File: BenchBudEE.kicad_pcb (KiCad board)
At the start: 4 copper layers, 165.1 x 63.5 mm, 111 parts, among them K1 RELAY, P1 24 Pin MiniFit JR, P2 CONN_2, P3 CONN_3X2, P4 12 Pin Terminal Block, P5 CONN_3, Q1 2N3904, Q2 MOSFET_N, Q3 NMOS, Q4 NMOS, SW1 SWITCH, U1 OPTO_TRANSISTOR, U10 LM317K, U2 MCP3901, U3 LMT84, U4 OPA4170, U5 AP5726, U6 MCP4801, U7 LM337T, U8 LM317K, U9 LM337T

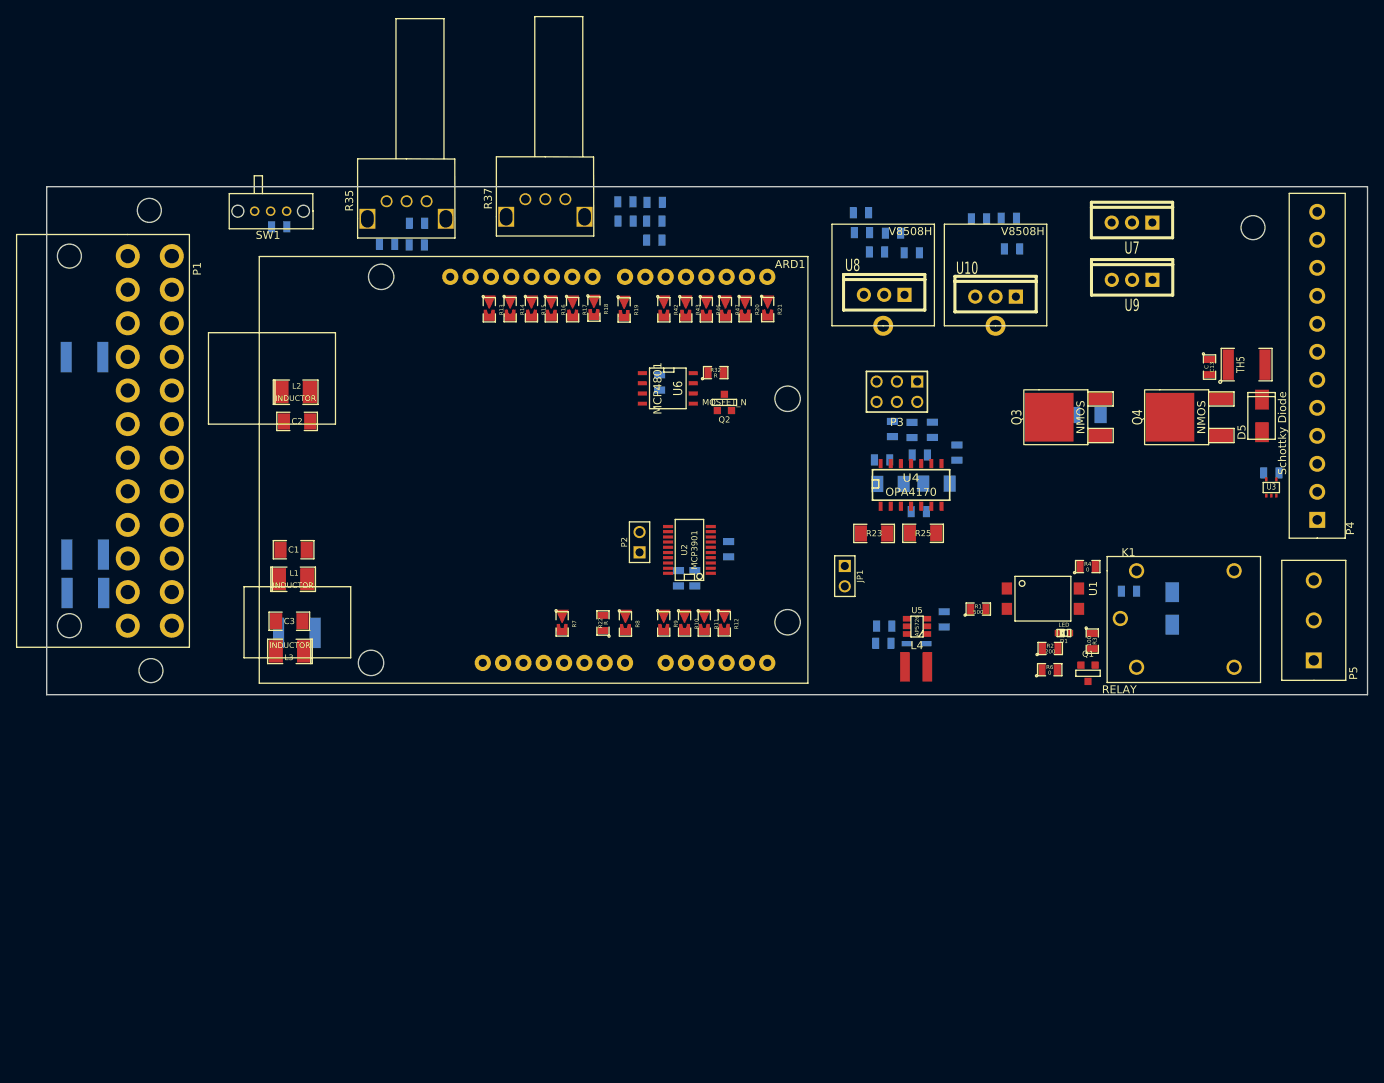
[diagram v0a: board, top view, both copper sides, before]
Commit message: Layout v4.0
Adding ground planes according to location of modules
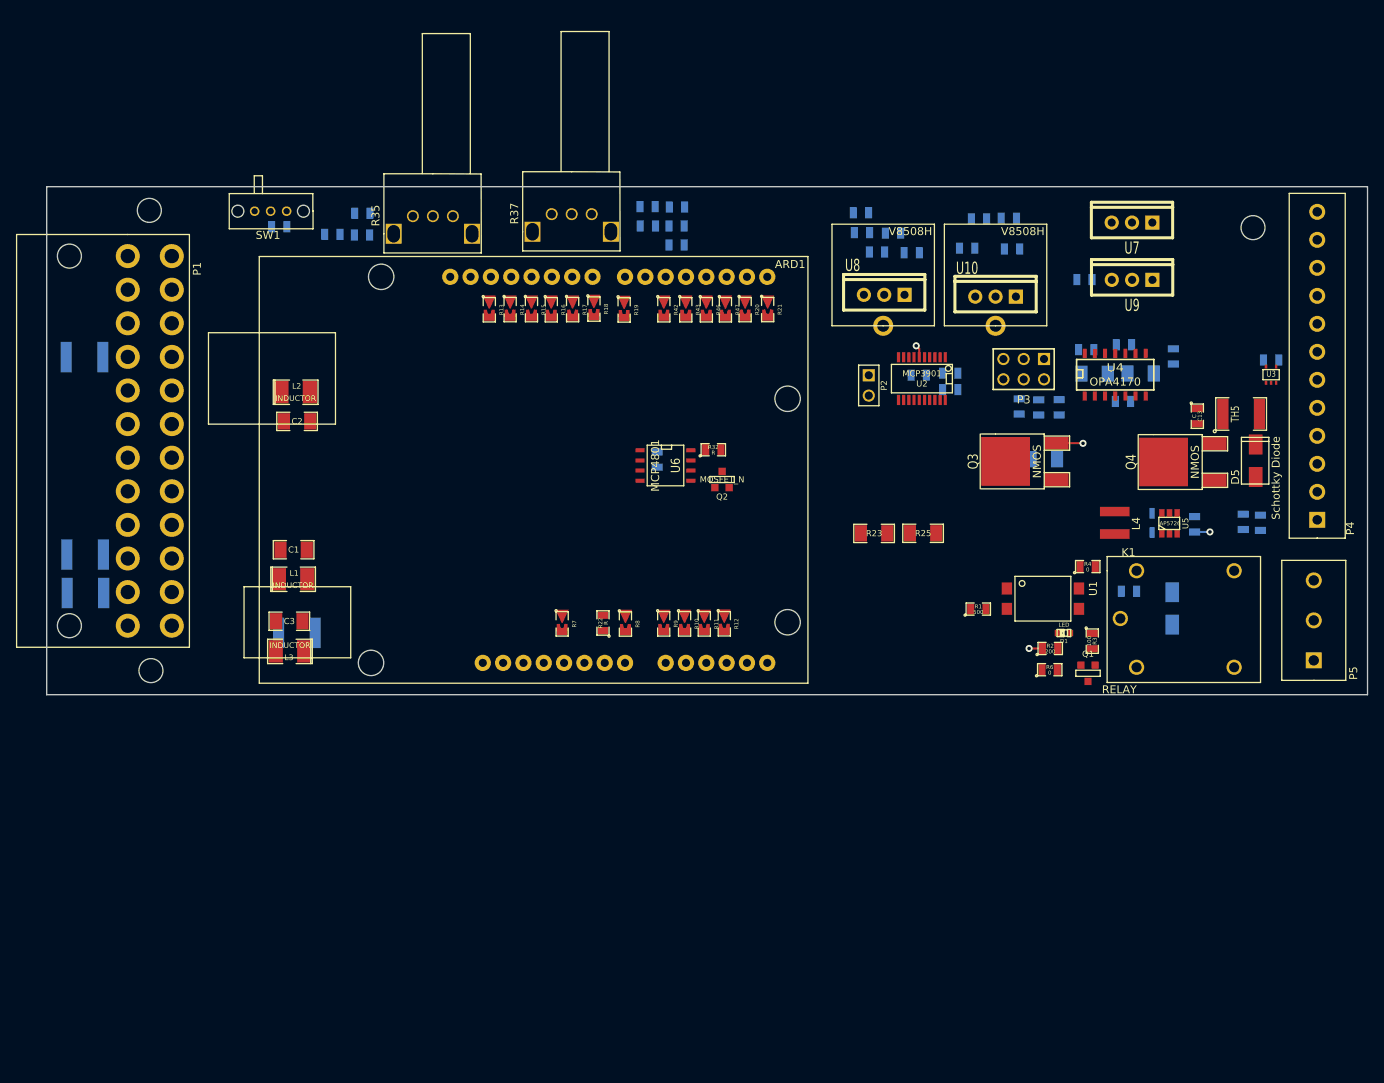
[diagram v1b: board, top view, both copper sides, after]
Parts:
- removed JP1: JUMPER, PIN_ARRAY_2X1
- added C20: C, SM0805, B.Cu at (182.3, 128.8)
- added C21: C, SM0805, B.Cu at (197.0, 132.7)
- moved C5 48.8 mm to (219.0, 163.1), turned to 90 degrees
- moved C4 47.5 mm to (216.9, 163.0), turned to 270 degrees
- moved C7 41.4 mm to (180.2, 146.5), turned to 0 degrees
- moved C6 40.9 mm to (180.2, 144.4), turned to 0 degrees
- moved U2 36.1 mm to (176.7, 145.1), turned to 180 degrees
- moved P2 34.7 mm to (170.0, 146.0), turned to 270 degrees
- moved U5 34.1 mm to (207.6, 163.2), turned to 0 degrees
- moved R31 33.5 mm to (210.8, 163.3)
- moved L4 32.6 mm to (200.8, 161.7), turned to 270 degrees
- moved C8 32.2 mm to (176.3, 144.7), turned to 180 degrees
- moved D4 31.5 mm to (205.5, 164.4), turned to 90 degrees
- moved R27 29.6 mm to (208.1, 142.3)
- moved R26 29.0 mm to (198.3, 144.5)
- moved U4 29.0 mm to (200.8, 144.5)
- moved C10 29.0 mm to (201.8, 148.0)
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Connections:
- C10 pad 2: AGND -> GND_TC
- C11 pad 2: AGND -> GND_TC
- C12 pad 2: AGND -> GND_FAN
- C13 pad 2: GND -> GND_FAN
- C14 pad 2: AGND -> GND_PWR
- C15 pad 2: AGND -> GND_PWR
- C16 pad 1: AGND -> GND_TC
- C17 pad 2: AGND -> GND_TC
- C18 pad 2: AGND -> GND_PWR
- C19 pad 2: AGND -> GND_PWR
- C4 pad 1: GND -> GND_LED
- C5 pad 2: GND -> GND_LED
- C6 pad 2: AGND -> GND_TC
- C7 pad 2: AGND -> GND_TC
- C8 pad 2: AGND -> GND_TC
- C9 pad 2: AGND -> GND_TC
- P4 pad 1: +3.3V -> /LED_Driver/LED+
- P4 pad 10: /Fan/TACH -> +5V
- P4 pad 11: /Terminal_Block/TC_IN_+ -> /Power_Adjustment_Monitor/V-_ADJ
- P4 pad 12: /Terminal_Block/TC_IN_- -> /Power_Adjustment_Monitor/V+_ADJ
- P4 pad 2: +5V -> /LED_Driver/LED-
- P4 pad 3: GND -> /Fan/TACH
- P4 pad 4: /Power_Adjustment_Monitor/V+_ADJ -> /Fan/PWR-
- P4 pad 5: /Power_Adjustment_Monitor/V-_ADJ -> /Fan/PWR+
- P4 pad 6: /LED_Driver/LED+ -> /Terminal_Block/TC_IN_-
- P4 pad 7: /LED_Driver/LED- -> /Terminal_Block/TC_IN_+
- P4 pad 8: /Fan/PWR+ -> GND
- P4 pad 9: /Fan/PWR- -> +3.3V
- Q2 pad S: AGND -> GND_FAN
- Q3 pad 3: GND -> GND_FAN
- R2 pad 1: GND -> GND_RELAY
- R24 pad 1: AGND -> GND_TC
- R31 pad 2: GND -> GND_LED
- R33 pad 2: GND -> GND_FAN
- R35 pad 2: AGND -> GND_PWR
- R37 pad 2: AGND -> GND_PWR
- R39 pad 2: AGND -> GND_PWR
- R41 pad 1: AGND -> GND_PWR
- R48 pad 2: AGND -> GND_TC
- R51 pad 2: AGND -> GND_TC
- R6 pad 1: GND -> GND_RELAY
- U2 pad 11: AGND -> GND_TC
- U2 pad 5: AGND -> GND_TC
- U2 pad 6: AGND -> GND_TC
- U2 pad 8: AGND -> GND_TC
- U3 pad 1: AGND -> GND_TC
- U3 pad 2: AGND -> GND_TC
- U3 pad 5: AGND -> GND_TC
- U5 pad 2: GND -> GND_LED
- U6 pad 7: AGND -> GND_FAN
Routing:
- net GND_FAN: track 0.00 -> 4.88 mm, vias 0 -> 1
- net GND_RELAY: track 0.00 -> 3.11 mm, vias 0 -> 1
- net GND_LED: track 0.00 -> 2.90 mm, vias 0 -> 1
- net GND_TC: track 0.00 -> 2.47 mm, vias 0 -> 1
- added copper zone on GND, net GND_FAN
- added copper zone on GND, net GND_LED
- added copper zone on GND, net GND_PWR
- added copper zone on GND, net GND_RELAY
- added copper zone on GND, net GND_TC

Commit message: Layout v5.0
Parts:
- added TP1: CONN_1, 1pin, F.Cu at (120.9, 160.5)
- C13, TH5: moved to B.Cu
- C4: moved to F.Cu
- moved C3 47.5 mm to (94.7, 128.0), turned to 0 degrees
- moved TH3 41.0 mm to (89.8, 179.3), turned to 0 degrees
- moved U9 33.2 mm to (169.8, 130.9), turned to 270 degrees
- moved U8 29.5 mm to (201.4, 136.4)
- moved C12 26.6 mm to (170.1, 153.8)
- moved R32 26.6 mm to (177.2, 152.6)
- moved U6 26.6 mm to (171.2, 154.6)
- moved Q2 26.6 mm to (178.2, 156.3)
- moved TH2 25.8 mm to (97.7, 163.7), turned to 0 degrees
- moved C2 18.3 mm to (94.7, 132.6)
- moved TH5 15.5 mm to (202.5, 155.9), turned to 90 degrees
- moved U7 15.2 mm to (213.7, 136.4)
- moved C13 14.3 mm to (198.9, 157.3), turned to 90 degrees
- moved C4 12.7 mm to (204.1, 163.7), turned to 90 degrees
- moved V8508H 11.6 mm to (183.8, 127.1), turned to 0 degrees
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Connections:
- C10 pad 2: GND_TC -> AGND
- C11 pad 2: GND_TC -> AGND
- C12 pad 2: GND_FAN -> AGND
- C13 pad 2: GND_FAN -> AGND
- C16 pad 1: GND_TC -> AGND
- C17 pad 2: GND_TC -> AGND
- C20 pad 2: GND_TC -> AGND
- C21 pad 1: GND_TC -> AGND
- C4 pad 2: +5V -> +5P
- C6 pad 2: GND_TC -> AGND
- C7 pad 2: GND_TC -> AGND
- C8 pad 2: GND_TC -> AGND
- C9 pad 2: GND_TC -> AGND
- L4 pad 1: +5V -> +5P
- P4 pad 8: GND -> GND_PWR
- Q2 pad S: GND_FAN -> AGND
- Q3 pad 3: GND_FAN -> AGND
- R24 pad 1: GND_TC -> AGND
- R33 pad 2: GND_FAN -> AGND
- R48 pad 2: GND_TC -> AGND
- R51 pad 2: GND_TC -> AGND
- U2 pad 11: GND_TC -> AGND
- U2 pad 5: GND_TC -> AGND
- U2 pad 6: GND_TC -> AGND
- U2 pad 8: GND_TC -> AGND
- U3 pad 1: GND_TC -> AGND
- U3 pad 2: GND_TC -> AGND
- U3 pad 5: GND_TC -> AGND
- U5 pad 6: +5V -> +5P
- U6 pad 7: GND_FAN -> AGND
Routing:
- net +12C: track 0.00 -> 205.3 mm, vias 0 -> 2
- net -12V: track 0.00 -> 134.0 mm, vias 0 -> 1
- net +12V: track 0.00 -> 112.5 mm, vias 0 -> 1
- net /Relay/RELAY_COM: track 0.00 -> 24.3 mm
- net /Relay/RELAY_NC: track 0.00 -> 10.5 mm
- net /Relay/RELAY_NO: track 0.00 -> 10.3 mm
- net +5P: track 0.00 -> 10.1 mm, vias 0 -> 1
- net AGND: track 0.00 -> 7.35 mm, vias 0 -> 2
- net GND_FAN: track 4.88 -> 0.00 mm, vias 1 -> 0
- net +12P: track 0.00 -> 3.22 mm, vias 0 -> 1
- net GND_TC: track 2.47 -> 0.00 mm, vias 1 -> 0
- net +5V: track 0.00 -> 1.42 mm, vias 0 -> 1
- net GND_LED: track 2.90 -> 1.94 mm
- added copper zone on PWR, net +12P
- added copper zone on PWR, net +5P
- added copper zone on PWR, net +5V
- added copper zone on GND, net AGND
- removed copper zone on GND, net GND_FAN
- removed copper zone on GND, net GND_TC

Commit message: Layout v6.0
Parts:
- added JP1: JUMPER, PIN_ARRAY_2X1, F.Cu at (125.7, 157.2)
- added JP2: JUMPER, PIN_ARRAY_2X1, F.Cu at (117.3, 164.8)
- added JP3: JUMPER, PIN_ARRAY_2X1, F.Cu at (118.6, 151.9)
- added JP4: JUMPER, PIN_ARRAY_2X1, F.Cu at (125.0, 164.6)
- C1, L1, U3: moved to B.Cu
- moved R48 114.2 mm to (220.0, 137.4), turned to 270 degrees
- moved C16 111.1 mm to (212.9, 142.0)
- moved R49 109.3 mm to (215.1, 138.9)
- moved L3 55.7 mm to (92.7, 123.7), turned to 0 degrees
- moved TH1 46.0 mm to (79.8, 124.5), turned to 0 degrees
- moved R50 38.8 mm to (206.5, 137.4), turned to 90 degrees
- moved R51 38.5 mm to (205.0, 134.1)
- moved C14 32.4 mm to (172.5, 134.1), turned to 270 degrees
- moved C17 31.7 mm to (202.2, 138.7)
- moved R40 25.2 mm to (168.7, 135.6)
- moved R41 25.2 mm to (165.4, 134.9), turned to 270 degrees
- moved C1 24.0 mm to (119.4, 156.5), turned to 0 degrees
- moved C19 23.6 mm to (168.7, 133.3)
- moved R36 20.0 mm to (164.3, 130.3), turned to 270 degrees
- moved C15 15.2 mm to (187.2, 134.1)
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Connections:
- P1 pad 1: N-0000098 -> N-00000100
- P1 pad 10: (no net) -> +12C
- P1 pad 12: (no net) -> N-00000100
- P1 pad 13: N-0000093 -> (no net)
- P1 pad 14: (no net) -> N-0000094
- P1 pad 15: N-0000096 -> (no net)
- P1 pad 16: (no net) -> N-0000098
- P1 pad 2: N-0000098 -> N-00000100
- P1 pad 3: N-0000095 -> N-00000109
- P1 pad 4: N-00000108 -> N-0000097
- P1 pad 5: N-0000095 -> GND
- P1 pad 6: GND -> N-0000097
- P1 pad 7: (no net) -> N-00000109
- P1 pad 8: N-00000108 -> (no net)
- P1 pad 9: +12C -> (no net)
- P4 pad 10: +5V -> +3.3V
- P4 pad 8: GND_PWR -> +5V
- P4 pad 9: +3.3V -> GND_PWR
- SW1 pad 2: N-0000096 -> N-0000098
- TH1 pad 1: N-0000098 -> N-00000100
- TH2 pad 1: N-0000095 -> N-0000097
- TH4 pad 1: N-0000093 -> N-0000094
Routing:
- net +3.3V: track 0.00 -> 155.6 mm
- net GND: track 0.00 -> 62.4 mm
- net N-0000097: track 0.00 -> 59.0 mm
- net -12P: track 0.00 -> 44.8 mm, vias 0 -> 1
- net +12P: track 3.22 -> 45.2 mm, vias 1 -> 2
- net N-00000120: track 0.00 -> 32.1 mm
- net +5V: track 1.42 -> 23.9 mm, vias 1 -> 2
- net +5P: track 10.1 -> 19.0 mm, vias 1 -> 2
- net N-00000100: track 0.00 -> 5.36 mm
- net N-0000094: track 0.00 -> 5.00 mm
- net +12C: track 205.3 -> 201.8 mm
- added copper zone on GND, net GND

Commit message: Layout v8.0
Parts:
- JP1, JP2, JP3, JP4: footprint PIN_ARRAY_2X1 -> GND_PNT
- R23, R25: moved to B.Cu
- moved C4 65.8 mm to (138.4, 163.6)
- moved C5 65.8 mm to (149.6, 165.0)
- moved L4 65.8 mm to (134.9, 162.4)
- moved R31 65.8 mm to (144.7, 164.0)
- moved U5 65.8 mm to (141.6, 163.8)
- moved D4 65.8 mm to (141.6, 165.1)
- moved R23 24.4 mm to (191.0, 150.9)
- moved R25 24.4 mm to (197.1, 150.9)
- moved C1 23.6 mm to (96.0, 152.9), turned to 90 degrees
- moved R32 7.69 mm to (169.5, 153.6)
- moved U6 7.69 mm to (163.6, 155.6)
- moved C12 7.69 mm to (162.5, 154.9)
- moved Q2 7.69 mm to (170.6, 157.3)
- moved C10 7.62 mm to (194.2, 148.0)
- moved P3 7.62 mm to (181.8, 143.9)
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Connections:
- R4 pad 2: +12V -> +12P
- R5 pad 2: +12V -> +12P
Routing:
- net /Arduino/RELAY+: track 0.00 -> 57.2 mm
- net /Arduino/RELAY-: track 0.00 -> 47.5 mm
- net +5P: track 19.0 -> 50.9 mm
- net +12P: track 45.2 -> 71.2 mm, vias 2 -> 4
- net N-0000086: track 0.00 -> 14.0 mm
- net N-0000091: track 0.00 -> 7.07 mm
- net N-0000083: track 0.00 -> 6.60 mm
- net +5V: track 23.9 -> 19.8 mm, vias 2 -> 3
- net N-0000037: track 0.00 -> 4.04 mm
- net N-0000089: track 0.00 -> 2.80 mm
- net GND_RELAY: track 3.11 -> 5.79 mm
- net N-0000090: track 0.00 -> 2.63 mm
- net N-0000082: track 0.00 -> 2.19 mm
- net N-0000085: track 0.00 -> 1.94 mm
- net +12C: track 201.8 -> 200.0 mm
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- added copper zone on F.Cu, net /Arduino/CURR_MEAS
- added copper zone on F.Cu, net /Fan/PWR-

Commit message: Layout v9.0
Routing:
- net N-00000123: track 0.00 -> 73.6 mm
- net /Power_Adjustment_Monitor/V-_ADJ: track 0.00 -> 73.5 mm, vias 0 -> 1
- net /Power_Adjustment_Monitor/V+_ADJ: track 0.00 -> 53.1 mm
- net AGND: track 5.81 -> 23.8 mm, vias 2 -> 7
- net +12V: track 112.5 -> 125.2 mm
- net GND_PWR: track 0.00 -> 12.6 mm, vias 0 -> 4
- net +3.3V: track 155.6 -> 167.4 mm
- net N-00000121: track 0.00 -> 6.35 mm
- net FE_V-: track 0.00 -> 5.95 mm
- net N-00000122: track 0.00 -> 5.41 mm
- net GND: track 60.9 -> 65.0 mm
- net +5V: track 19.8 -> 23.0 mm, vias 3 -> 4
- net N-00000120: track 30.4 -> 33.5 mm
- net -12V: track 134.0 -> 131.3 mm
- net /Arduino/V-_ADJ_MON: track 0.00 -> 2.43 mm
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
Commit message: Layout v10.0
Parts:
- ARD1: moved to B.Cu
- R31: moved to F.Cu
- moved C5 74.1 mm to (223.6, 163.8), turned to 270 degrees
- moved L4 12.8 mm to (147.7, 162.8)
- moved D4 10.6 mm to (152.2, 165.5)
- moved C4 5.41 mm to (133.0, 164.2), turned to 270 degrees
- moved U5 3.88 mm to (137.7, 164.2), turned to 90 degrees
- moved R31 2.68 mm to (142.0, 164.1)
- turned ARD1 to 270 degrees
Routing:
- net /LED_Driver/LED+: track 0.00 -> 96.5 mm, vias 0 -> 1
- net /LED_Driver/LED-: track 0.00 -> 90.4 mm, vias 0 -> 1
- net /Arduino/LED_EN_PWM: track 0.00 -> 26.8 mm
- net N-00000116: track 0.00 -> 15.4 mm, vias 0 -> 1
- net GND_LED: track 1.94 -> 9.12 mm, vias 1 -> 3
- net +5P: track 50.9 -> 49.9 mm

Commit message: Layout v11.0
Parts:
- added L5: INDUCTOR, SM0805, B.Cu at (174.1, 142.1)
- ARD1, R24, R26, R27, R28, R29, R33, R44, R45: moved to F.Cu
- Q2, R32: moved to B.Cu
- moved C16 26.9 mm to (186.3, 146.2), turned to 90 degrees
- moved R28 24.5 mm to (205.7, 147.5), turned to 0 degrees
- moved R33 22.9 mm to (165.3, 150.4)
- moved R44 22.3 mm to (205.6, 144.9), turned to 0 degrees
- moved R45 20.3 mm to (205.6, 142.5), turned to 0 degrees
- moved C17 20.3 mm to (183.4, 146.3), turned to 270 degrees
- moved P3 19.1 mm to (200.8, 145.0), turned to 270 degrees
- moved R24 19.0 mm to (178.4, 140.6), turned to 90 degrees
- moved Q3 18.5 mm to (171.7, 150.3), turned to 180 degrees
- moved U6 18.5 mm to (145.1, 154.7)
- moved R27 18.3 mm to (190.1, 148.9), turned to 90 degrees
- moved C12 16.7 mm to (145.8, 153.7), turned to 180 degrees
- moved R25 12.3 mm to (184.8, 150.9), turned to 270 degrees
- moved Q2 12.0 mm to (176.2, 146.7), turned to 270 degrees
- moved R23 11.7 mm to (185.3, 140.6), turned to 270 degrees
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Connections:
- C6 pad 1: +5V -> N-0000070
- P4 pad 6: /Terminal_Block/TC_IN_- -> /Terminal_Block/TC_IN_+
- P4 pad 7: /Terminal_Block/TC_IN_+ -> /Terminal_Block/TC_IN_-
- R14 pad 2: /Arduino/MISO -> /Arduino/MOSI
- R15 pad 2: /Arduino/MOSI -> /Arduino/MISO
- U2 pad 2: +5V -> N-0000070
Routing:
- net N-0000068: track 0.00 -> 56.7 mm, vias 0 -> 1
- net /Terminal_Block/TC_IN_-: track 0.00 -> 44.9 mm, vias 0 -> 1
- net /Terminal_Block/TC_IN_+: track 0.00 -> 41.8 mm, vias 0 -> 1
- net /Arduino/CURR_MEAS: track 0.00 -> 33.4 mm
- net N-00000118: track 0.00 -> 30.4 mm, vias 0 -> 1
- net FE_V-: track 5.95 -> 35.7 mm, vias 0 -> 1
- net FE_V+: track 2.36 -> 30.0 mm, vias 0 -> 1
- net N-0000078: track 0.00 -> 26.4 mm
- net N-00000119: track 0.00 -> 25.9 mm
- net AGND: track 23.8 -> 48.4 mm, vias 7 -> 12
- net /Arduino/FAN_MODE: track 0.00 -> 24.2 mm
- net N-0000076: track 0.00 -> 23.8 mm, vias 0 -> 4
- net N-0000082: track 0.00 -> 17.3 mm
- net /Fan/PWR+: track 0.00 -> 14.7 mm, vias 0 -> 1
- net N-0000072: track 0.00 -> 11.5 mm
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
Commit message: Layout v12.0
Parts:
- C12: moved to F.Cu
- R10, R11, R12, R16, R17, R18, R19, R42, R9: moved to B.Cu
- moved R33 19.3 mm to (183.0, 158.0)
- moved C12 14.2 mm to (160.0, 155.0), turned to 270 degrees
- moved R20 12.5 mm to (142.6, 137.3)
- moved U6 10.9 mm to (156.0, 154.8), turned to 180 degrees
- moved C8 6.25 mm to (164.6, 138.1)
- moved P2 5.64 mm to (165.4, 148.7), turned to 180 degrees
- moved R22 4.71 mm to (137.4, 171.7)
- moved R42 0.15 mm to (145.1, 137.3)
- moved R9 0.13 mm to (145.1, 176.6)
- moved R16 0.08 mm to (130.9, 137.2)
- moved R18 0.06 mm to (136.2, 137.2)
- moved R43 0.06 mm to (147.6, 137.3)
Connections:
- ARD1 pad 12: N-0000052 (its old number) -> (no net)
- ARD1 pad 17: (no net) -> N-0000047
- P1 pad 3: N-00000110 -> GND
- P1 pad 7: N-00000110 -> GND
- R20 pad 1: N-0000052 (its old number) -> N-0000047
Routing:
- net /Arduino/V+_ADJ_MON: track 2.17 -> 146.3 mm, vias 0 -> 2
- net /Arduino/V-_ADJ_MON: track 2.43 -> 119.9 mm, vias 0 -> 2
- net /Fan/TACH: track 0.00 -> 94.4 mm
- net /Arduino/SCLK: track 0.00 -> 65.7 mm, vias 0 -> 2
- net /Arduino/FAN_PWM: track 0.00 -> 63.7 mm
- net /Arduino/MOSI: track 0.00 -> 62.8 mm, vias 0 -> 3
- net N-0000099: track 0.00 -> 57.2 mm
- net N-00000101: track 5.36 -> 58.6 mm
- net /Arduino/MISO: track 0.00 -> 51.0 mm, vias 0 -> 2
- net +5V: track 27.1 -> 73.8 mm, vias 4 -> 5
- net /Arduino/CURR_MEAS: track 33.4 -> 77.8 mm, vias 0 -> 1
- net /Arduino/~ADC_CS: track 0.00 -> 40.7 mm, vias 0 -> 1
- net GND: track 65.0 -> 104.5 mm, vias 1 -> 3
- net /Arduino/~RESET: track 0.00 -> 32.6 mm, vias 0 -> 1
- net /Fan/~CS: track 0.00 -> 29.8 mm, vias 0 -> 1
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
